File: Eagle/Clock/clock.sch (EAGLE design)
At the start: 26 parts

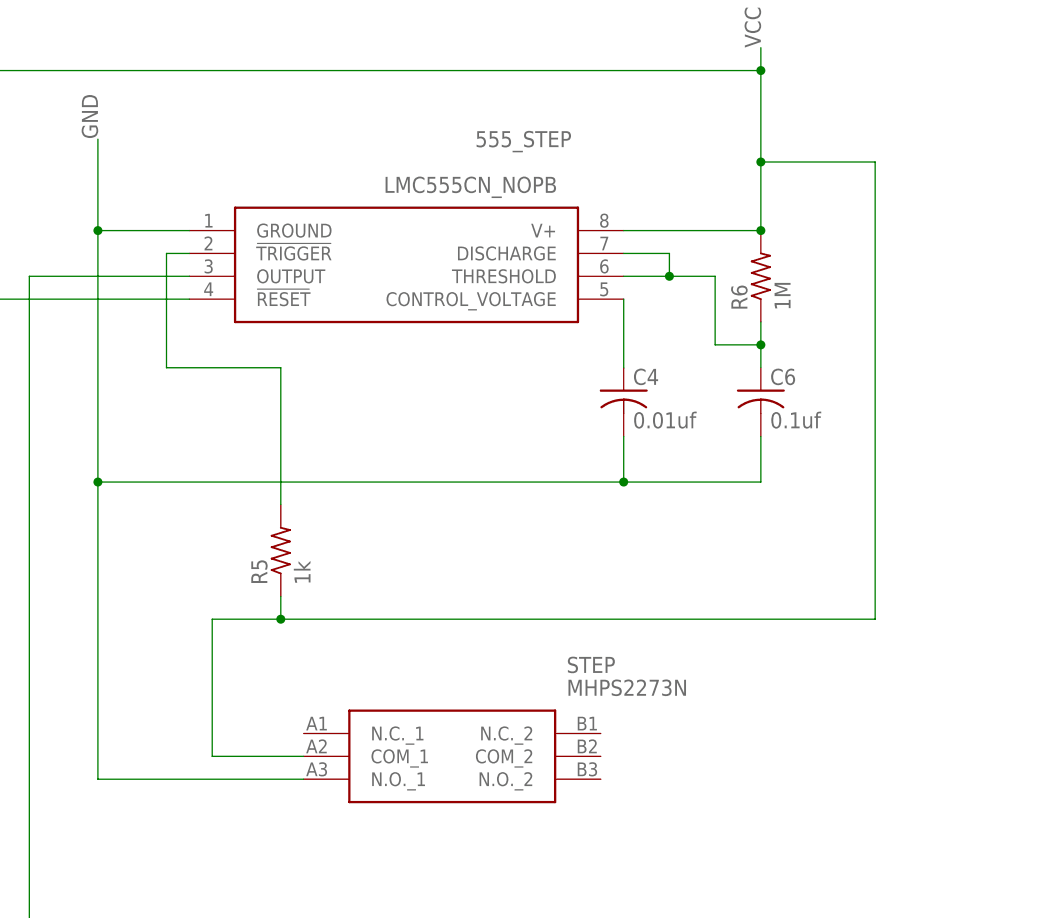
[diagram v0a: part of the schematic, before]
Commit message: started adding revision 2 to fix errors in first set of boards
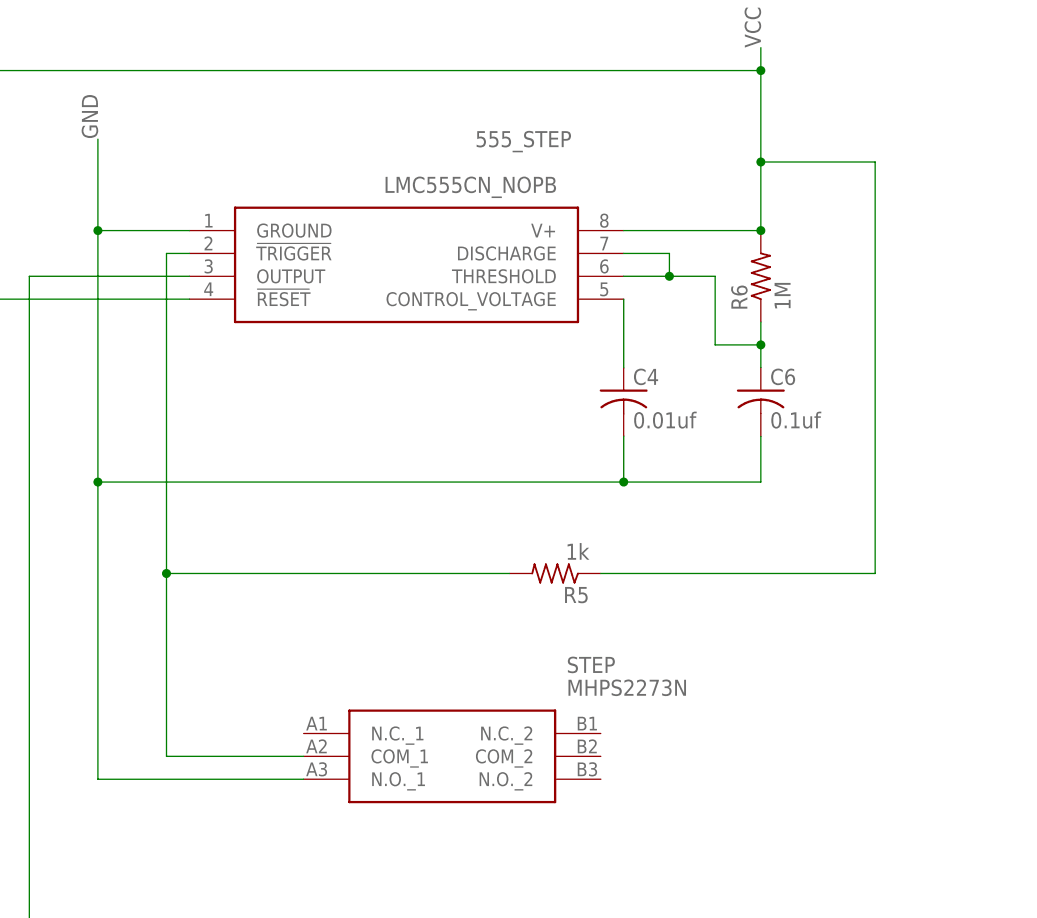
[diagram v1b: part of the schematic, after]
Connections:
- net N$7: now also STEP.COM_1
- net VCC: no longer STEP.COM_1
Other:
- moved on the sheet: R5
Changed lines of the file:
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@@
 <attribute name="VALUE" x="285.242" y="67.31" size="1.778" layer="96" rot="R90"/>
 </instance>
-<instance part="R5" gate="G$1" x="160.02" y="25.4" smashed="yes" rot="R90">
-<attribute name="NAME" x="158.5214" y="21.59" size="1.778" layer="95" rot="R90"/>
-<attribute name="VALUE" x="163.322" y="21.59" size="1.778" layer="96" rot="R90"/>
+<instance part="R5" gate="G$1" x="190.5" y="22.86" smashed="yes" rot="R180">
+<attribute name="NAME" x="194.31" y="21.3614" size="1.778" layer="95" rot="R180"/>
+<attribute name="VALUE" x="194.31" y="26.162" size="1.778" layer="96" rot="R180"/>
 </instance>
 <instance part="R6" gate="G$1" x="213.36" y="55.88" smashed="yes" rot="R90">
@@
 <junction x="213.36" y="78.74"/>
 <wire x1="213.36" y1="68.58" x2="226.06" y2="68.58" width="0.1524" layer="91"/>
-<wire x1="226.06" y1="68.58" x2="226.06" y2="17.78" width="0.1524" layer="91"/>
+<wire x1="226.06" y1="68.58" x2="226.06" y2="22.86" width="0.1524" layer="91"/>
 <junction x="213.36" y="68.58"/>
-<wire x1="226.06" y1="17.78" x2="160.02" y2="17.78" width="0.1524" layer="91"/>
 <pinref part="R5" gate="G$1" pin="1"/>
-<wire x1="160.02" y1="17.78" x2="160.02" y2="20.32" width="0.1524" layer="91"/>
-<wire x1="160.02" y1="17.78" x2="152.4" y2="17.78" width="0.1524" layer="91"/>
-<junction x="160.02" y="17.78"/>
-<pinref part="STEP" gate="G$1" pin="COM_1"/>
-<wire x1="152.4" y1="17.78" x2="152.4" y2="2.54" width="0.1524" layer="91"/>
-<wire x1="152.4" y1="2.54" x2="162.56" y2="2.54" width="0.1524" layer="91"/>
+<wire x1="195.58" y1="22.86" x2="226.06" y2="22.86" width="0.1524" layer="91"/>
 </segment>
 <segment>
@@
 </segment>
 </net>
-<net name="N$7" class="0">
-<segment>
-<pinref part="555_STEP" gate="G$1" pin="!TRIGGER"/>
-<wire x1="149.86" y1="58.42" x2="147.32" y2="58.42" width="0.1524" layer="91"/>
-<wire x1="147.32" y1="58.42" x2="147.32" y2="45.72" width="0.1524" layer="91"/>
-<pinref part="R5" gate="G$1" pin="2"/>
-<wire x1="160.02" y1="30.48" x2="160.02" y2="45.72" width="0.1524" layer="91"/>
-<wire x1="160.02" y1="45.72" x2="147.32" y2="45.72" width="0.1524" layer="91"/>
-</segment>
-</net>
 <net name="N$8" class="0">
 <segment>
@@
 </segment>
 </net>
+<net name="N$7" class="0">
+<segment>
+<pinref part="STEP" gate="G$1" pin="COM_1"/>
+<wire x1="147.32" y1="2.54" x2="162.56" y2="2.54" width="0.1524" layer="91"/>
+<pinref part="555_STEP" gate="G$1" pin="!TRIGGER"/>
+<wire x1="149.86" y1="58.42" x2="147.32" y2="58.42" width="0.1524" layer="91"/>
+<wire x1="147.32" y1="2.54" x2="147.32" y2="22.86" width="0.1524" layer="91"/>
+<pinref part="R5" gate="G$1" pin="2"/>
+<wire x1="147.32" y1="22.86" x2="147.32" y2="58.42" width="0.1524" layer="91"/>
+<wire x1="185.42" y1="22.86" x2="147.32" y2="22.86" width="0.1524" layer="91"/>
+<junction x="147.32" y="22.86"/>
+</segment>
+</net>
